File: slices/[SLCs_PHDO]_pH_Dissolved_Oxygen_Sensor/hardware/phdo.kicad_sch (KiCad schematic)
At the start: 21 parts, among them J2 Conn_01x05_Female, J3 Conn_01x05_Female, J4 Conn_01x03_Male, J5 Conn_01x03_Male, J6 Conn_01x03_Male, J7 Conn_01x03_Male

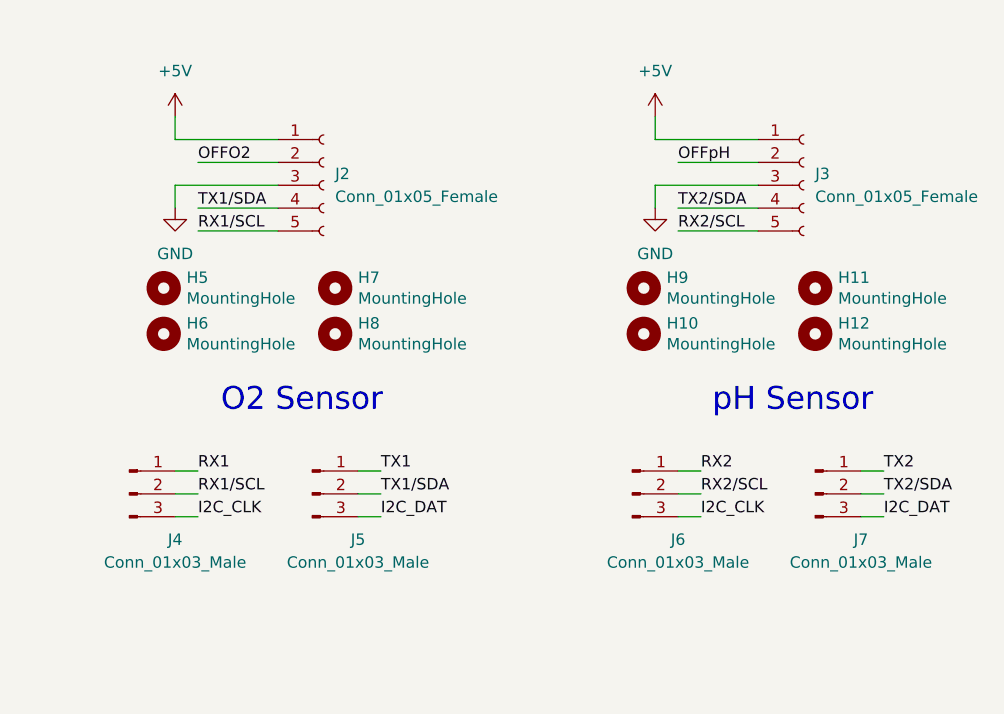
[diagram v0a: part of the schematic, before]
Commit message: restructuring for rpi boards
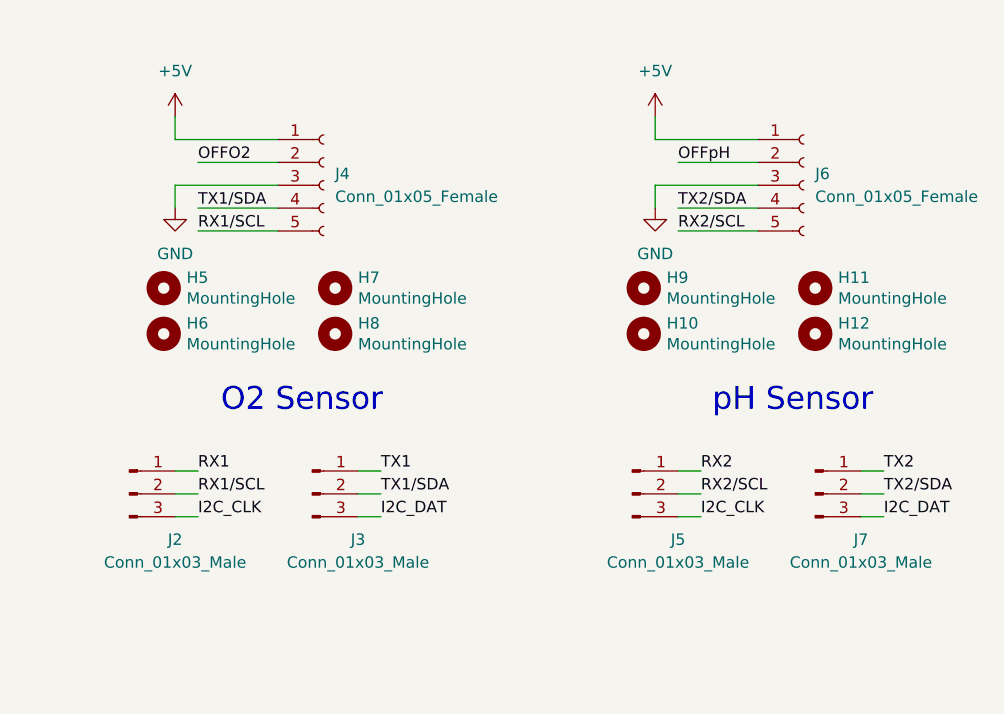
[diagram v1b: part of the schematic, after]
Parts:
- renumbered J4 to J2, J5 to J3, J2 to J4, J6 to J5, J3 to J6
